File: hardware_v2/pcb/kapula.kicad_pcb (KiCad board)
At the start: 4 copper layers, 50 x 59 mm, 166 parts, among them J1 Conn_02x10_Odd_Even, J2 Conn_02x10_Odd_Even, J3 U.FL, J4 U.FL, J5 U.FL, J6 U.FL, Q1 AO3401A, Q2 AO3400A, Q3 AO3400A, Q4 AO3400A, Q5 AO3401A, Q6 BSS84, T1 BW21S7511A01TF, T2 BW21S7511A01TF, T3 BW21S7511A01TF, T4 BW21S7511A01TF, U1 TP4054, U2 DW01+G, U3 XC6206P332MR, U4 FM8002A, U5 EFR32FG14P233F256GM48-B, U6 TG2016SMN 38.4000M-MCGNNM3, U7 XA213-G4J, Y1 32768 Hz

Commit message: PCB: Commit some changes
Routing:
- net /RESET: track 49.9 -> 49.4 mm
- net GND: vias 378 -> 381

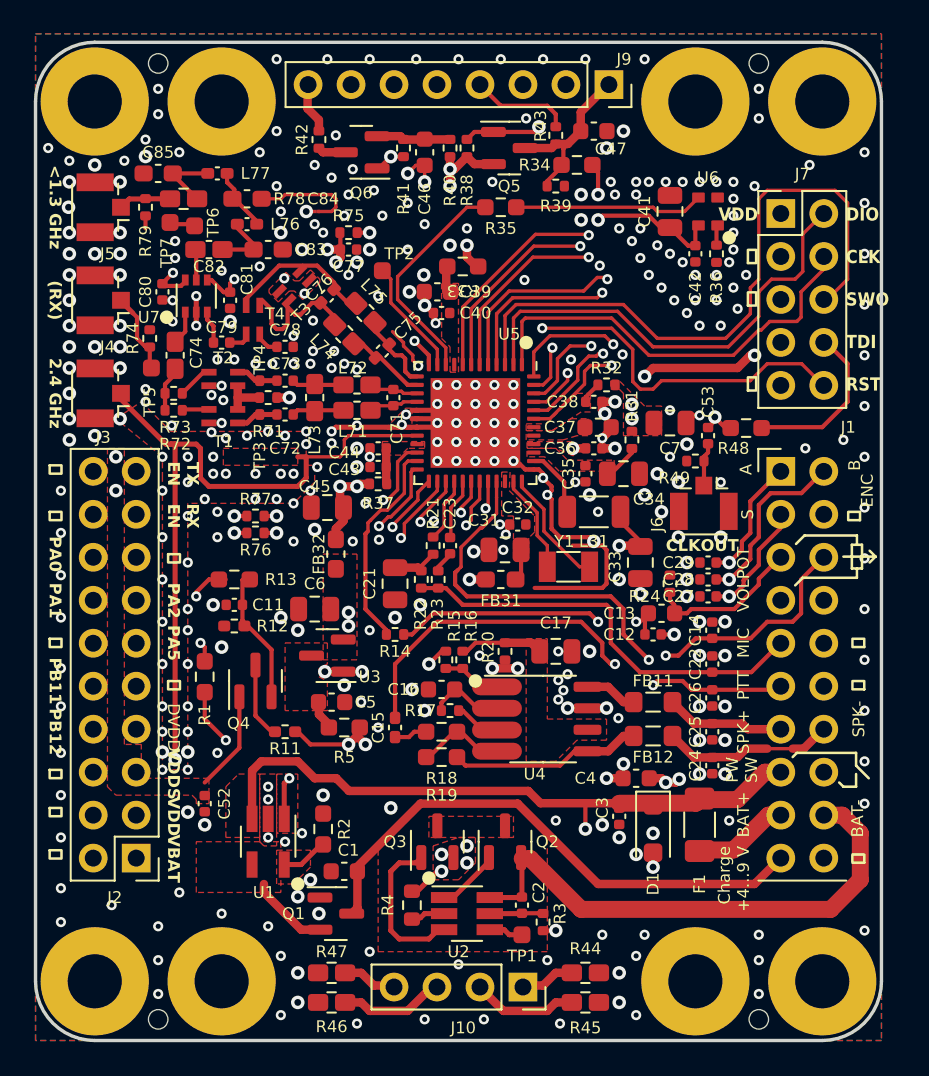
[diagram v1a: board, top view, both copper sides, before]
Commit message: PCB: Change some RF matching footprints, improve silkscreen
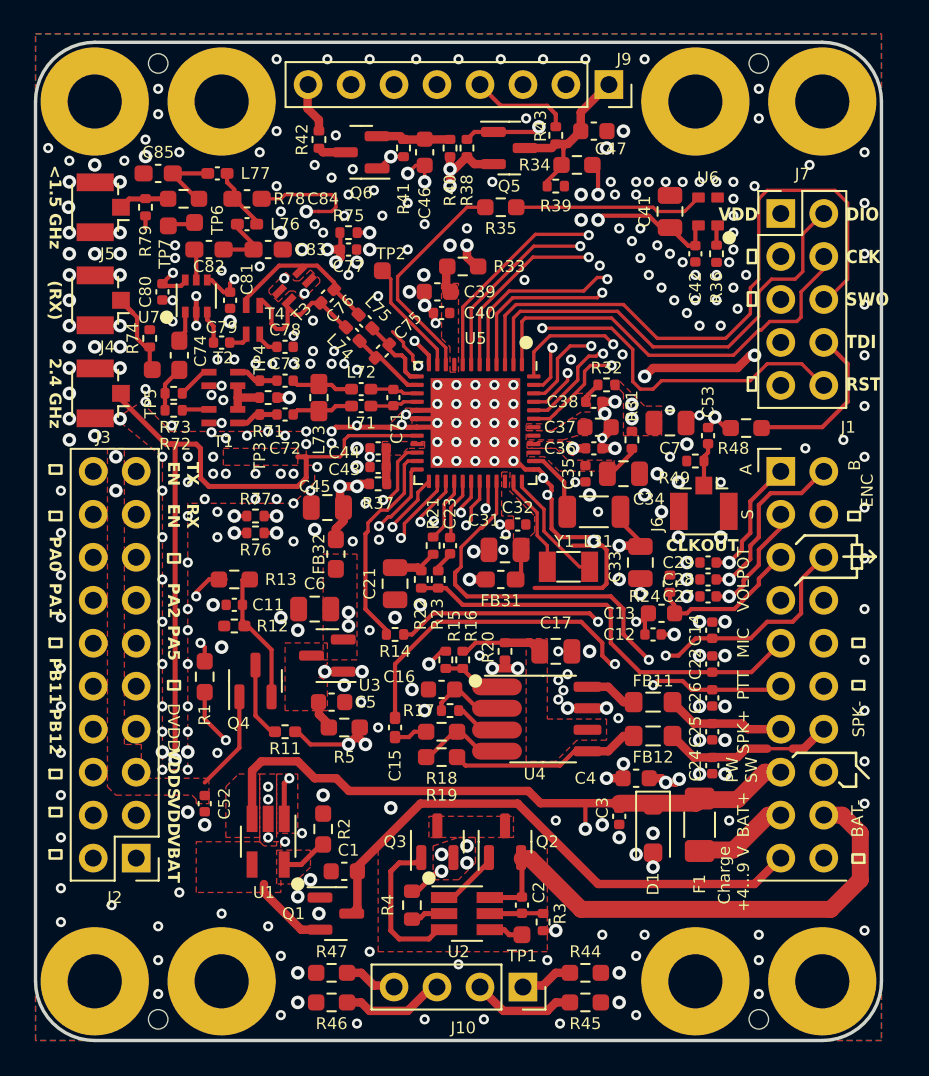
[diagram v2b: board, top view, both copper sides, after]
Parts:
- C74, C82: footprint kapula:C_0402_to_0603_HandSolder -> Capacitor_SMD:C_0603_1608Metric_Pad1.08x0.95mm_HandSolder
- L71, L72, L74, L75: footprint kapula:L_0402_to_0603_HandSolder -> Inductor_SMD:L_0402_1005Metric_Pad0.77x0.64mm_HandSolder
- R44, R45, R46, R47, R78: footprint kapula:R_0402_to_0603_HandSolder -> Resistor_SMD:R_0603_1608Metric_Pad0.98x0.95mm_HandSolder
- moved L74 0.50 mm to (118.8, 74.8)
- moved L75 0.50 mm to (119.5, 74.0)
- moved L71 0.35 mm to (119.2, 79.0)
- moved L72 0.35 mm to (119.2, 78.0)
- moved C74 0.25 mm to (108.5, 76.0)
- moved L73 0.25 mm to (116.8, 78.5)
- moved TP7 0.22 mm to (107.8, 68.3)
- moved TP6 0.20 mm to (109.4, 68.2)
- moved TP5 0.11 mm to (106.9, 76.8)
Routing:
- net Net-(C73-Pad2): track 3.07 -> 3.65 mm
- net Net-(C72-Pad2): track 3.07 -> 3.65 mm
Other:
- board text added: "<1.5 GHz"
- board text added: "JLCJLCJLCJLC"
- board text removed: "<1.3 GHz"

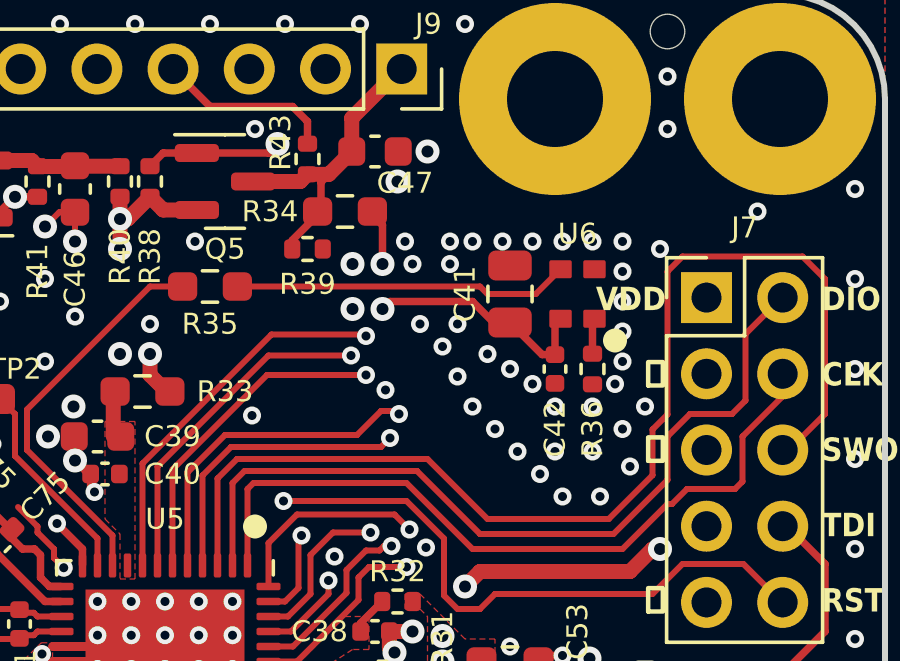
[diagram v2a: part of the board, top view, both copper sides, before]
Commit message: PCB: Cleanup layout around TCXO
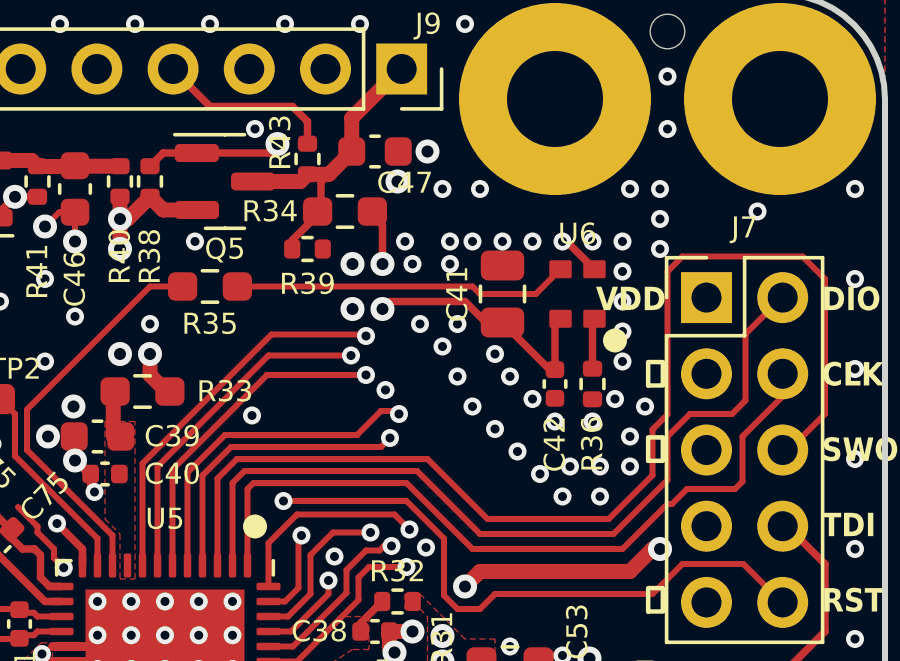
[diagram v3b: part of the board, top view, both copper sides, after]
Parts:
- moved C42 0.50 mm to (139.0, 70.5)
- moved R36 0.50 mm to (140.2, 70.5)
- moved C41 0.25 mm to (137.2, 67.5)
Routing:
- net GND: track 61.5 -> 62.9 mm, vias 381 -> 386
- net /TCXOVDD: track 11.3 -> 12.0 mm
- net Net-(U6-EN): track 1.19 -> 1.69 mm

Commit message: PCB: Rename net 1V8 to DVDD
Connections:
- net /1V8 renamed /DVDD
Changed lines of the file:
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@@
   (net 10 "/SWO_TDO")
   (net 11 "/PF3_TDI")
-  (net 12 "/1V8")
+  (net 12 "/DVDD")
   (net 13 "/EFR_AVDD")
   (net 14 "/PAVDD_2G4")
@@
       (stroke (width 0.1) (type solid)) (layer "F.Fab"))
     (pad "1" smd roundrect (at -0.95 0 270) (size 1 1.45) (layers "F.Cu" "F.Paste" "F.Mask") (roundrect_rratio 0.25)
-      (net 12 "/1V8") (pintype "passive"))
+      (net 12 "/DVDD") (pintype "passive"))
     (pad "2" smd roundrect (at 0.95 0 270) (size 1 1.45) (layers "F.Cu" "F.Paste" "F.Mask") (roundrect_rratio 0.25)
       (net 2 "GND") (pintype "passive"))
@@
       (net 98 "/EFR_VREGSW") (pinfunction "1") (pintype "passive"))
     (pad "2" smd roundrect (at 1.575 0) (size 1.05 1.9) (layers "F.Cu" "F.Paste" "F.Mask") (roundrect_rratio 0.2380952381)
-      (net 12 "/1V8") (pinfunction "2") (pintype "passive"))
+      (net 12 "/DVDD") (pinfunction "2") (pintype "passive"))
     (model "${KICAD6_3DMODEL_DIR}/Inductor_SMD.3dshapes/L_1206_3216Metric.wrl"
       (offset (xyz 0 0 0))
@@
       (stroke (width 0.1) (type solid)) (layer "F.Fab"))
     (pad "1" smd roundrect (at -0.48 0) (size 0.56 0.62) (layers "F.Cu" "F.Paste" "F.Mask") (roundrect_rratio 0.25)
-      (net 12 "/1V8") (pintype "passive"))
+      (net 12 "/DVDD") (pintype "passive"))
     (pad "2" smd roundrect (at 0.48 0) (size 0.56 0.62) (layers "F.Cu" "F.Paste" "F.Mask") (roundrect_rratio 0.25)
       (net 2 "GND") (pintype "passive"))
@@
       (net 23 "/EFR_VREGVDD") (pinfunction "VREGVDD") (pintype "power_in"))
     (pad "40" smd roundrect (at 1.25 -3.45 270) (size 0.25 0.8) (layers "F.Cu" "F.Paste" "F.Mask") (roundrect_rratio 0.25)
-      (net 12 "/1V8") (pinfunction "DVDD") (pintype "power_in"))
+      (net 12 "/DVDD") (pinfunction "DVDD") (pintype "power_in"))
     (pad "41" smd roundrect (at 0.75 -3.45 270) (size 0.25 0.8) (layers "F.Cu" "F.Paste" "F.Mask") (roundrect_rratio 0.25)
       (net 37 "/EFR_DECOUPLE") (pinfunction "DECOUPLE") (pintype "passive"))
@@
       (stroke (width 0.1) (type solid)) (layer "F.Fab"))
     (pad "1" smd roundrect (at -0.9125 0 180) (size 0.975 0.95) (layers "F.Cu" "F.Paste" "F.Mask") (roundrect_rratio 0.25)
-      (net 12 "/1V8") (pintype "passive"))
+      (net 12 "/DVDD") (pintype "passive"))
     (pad "2" smd roundrect (at 0.9125 0 180) (size 0.975 0.95) (layers "F.Cu" "F.Paste" "F.Mask") (roundrect_rratio 0.25)
       (net 60 "/RFVDD") (pintype "passive"))
@@
       (net 2 "GND") (pinfunction "Pin_6") (pintype "passive"))
     (pad "7" thru_hole oval (at 0 7.62 180) (size 1.7 1.7) (drill 1) (layers "*.Cu" "*.Mask")
-      (net 12 "/1V8") (pinfunction "Pin_7") (pintype "passive"))
+      (net 12 "/DVDD") (pinfunction "Pin_7") (pintype "passive"))
     (pad "8" thru_hole oval (at 2.54 7.62 180) (size 1.7 1.7) (drill 1) (layers "*.Cu" "*.Mask")
       (net 107 "/PB12") (pinfunction "Pin_8") (pintype "passive"))
@@
     )
   )
-  (zone (net 12) (net_name "/1V8") (layer "F.Cu") (hatch edge 0.5)
+  (zone (net 12) (net_name "/DVDD") (layer "F.Cu") (hatch edge 0.5)
     (priority 7)
     (connect_pads yes (clearance 0.15))
